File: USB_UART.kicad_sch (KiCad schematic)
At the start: 2 parts, among them U4 FT232RL

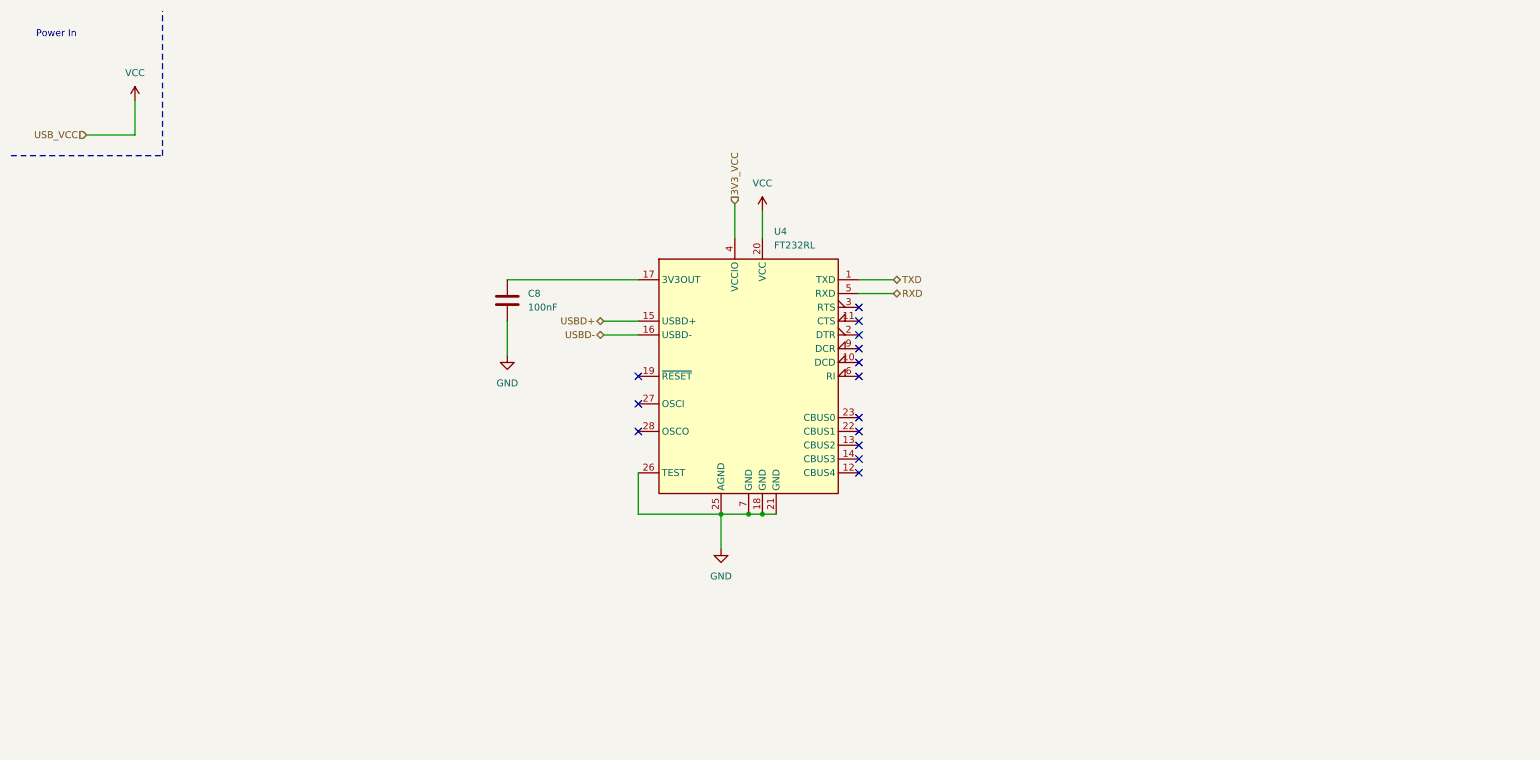
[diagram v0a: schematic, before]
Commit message: feat(usb-uart): add FT232RL for USB-serial, update schematic and layout
Added FT232RL USB‑to‑UART interface IC, powered from 3.3 V and 5 V rails. Connected RXD and TXD to MCU via hierarchical sheet. Left RS‑232 control lines and CBUS pins unconnected. Updated hierarchy with USB_UART sheet pins.

BREAKING CHANGE: USB connector moved to USB_UART sheet; schematic wiring changed to bus-based layout. AGND now kept in separate plane using GNDA power symbol in KiCad.
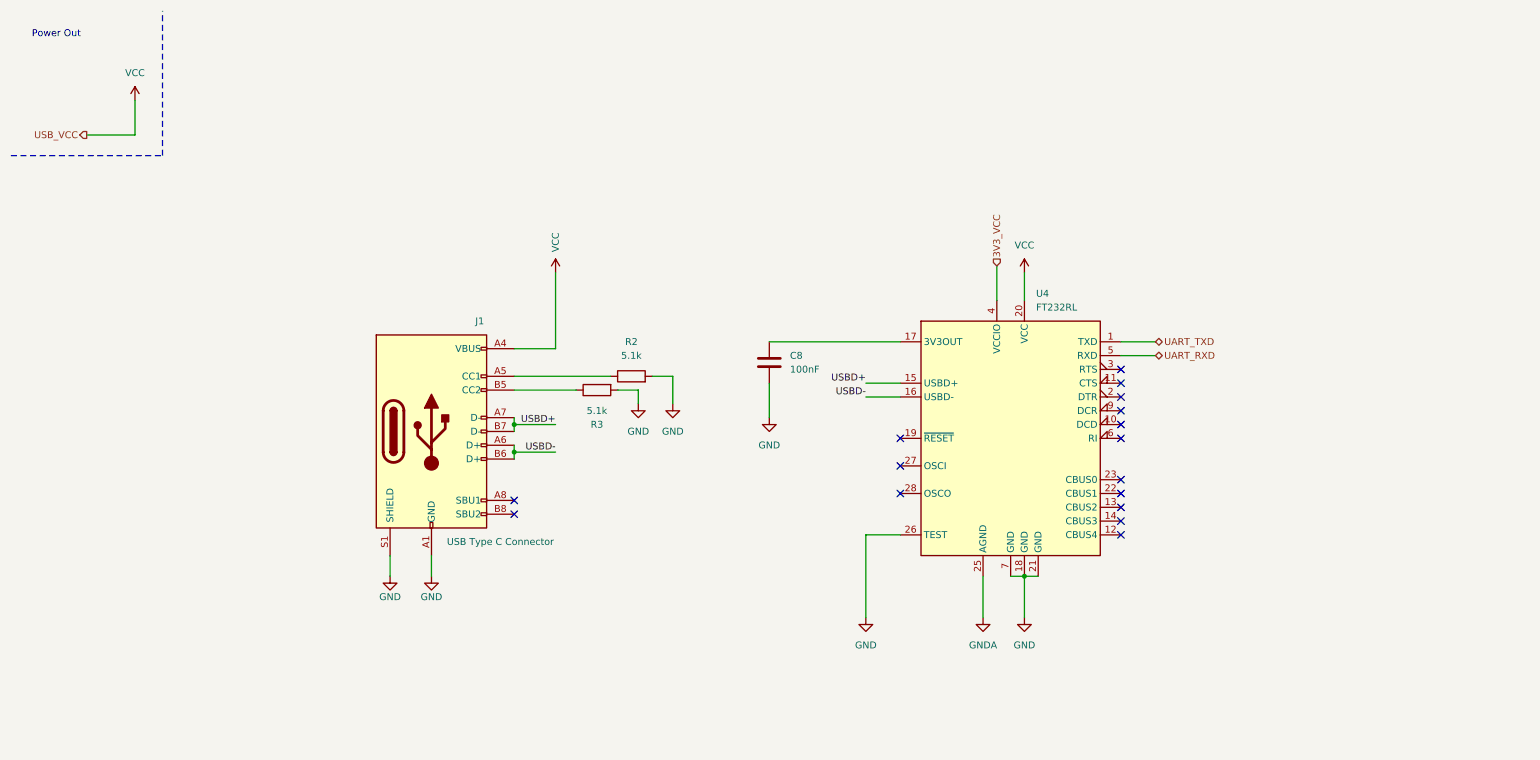
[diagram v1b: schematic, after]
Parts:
- added J1: USB Type C Connector, symbol Connector:USB_C_Receptacle_USB2.0_16P
- added R2, R3: 5.1k, symbol Device:R
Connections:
- net GND: now also J1.A1 (GND), J1.A12 (GND), J1.B1 (GND), J1.B12 (GND), J1.S1 (SHIELD), R2.2, R3.2; no longer U4.25 (AGND)
- net USBD+: now also J1.A7 (D-), J1.B7 (D-)
- net USBD-: now also J1.A6 (D+), J1.B6 (D+)
- net VCC: now also J1.A4 (VBUS), J1.A9 (VBUS), J1.B4 (VBUS), J1.B9 (VBUS)
- net RXD renamed UART_RXD
- net TXD renamed UART_TXD
- new net: J1.A5 (CC1), R2.1
- new net: J1.B5 (CC2), R3.1
- new net GNDA: U4.25 (AGND)
- no-connect marks 14 -> 16
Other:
- note added: "Power Out"
- note removed: "Power In"
- moved on the sheet: C8, U4

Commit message: fix: Separted CC1 and CC2 resistors and fixed the UART label directions
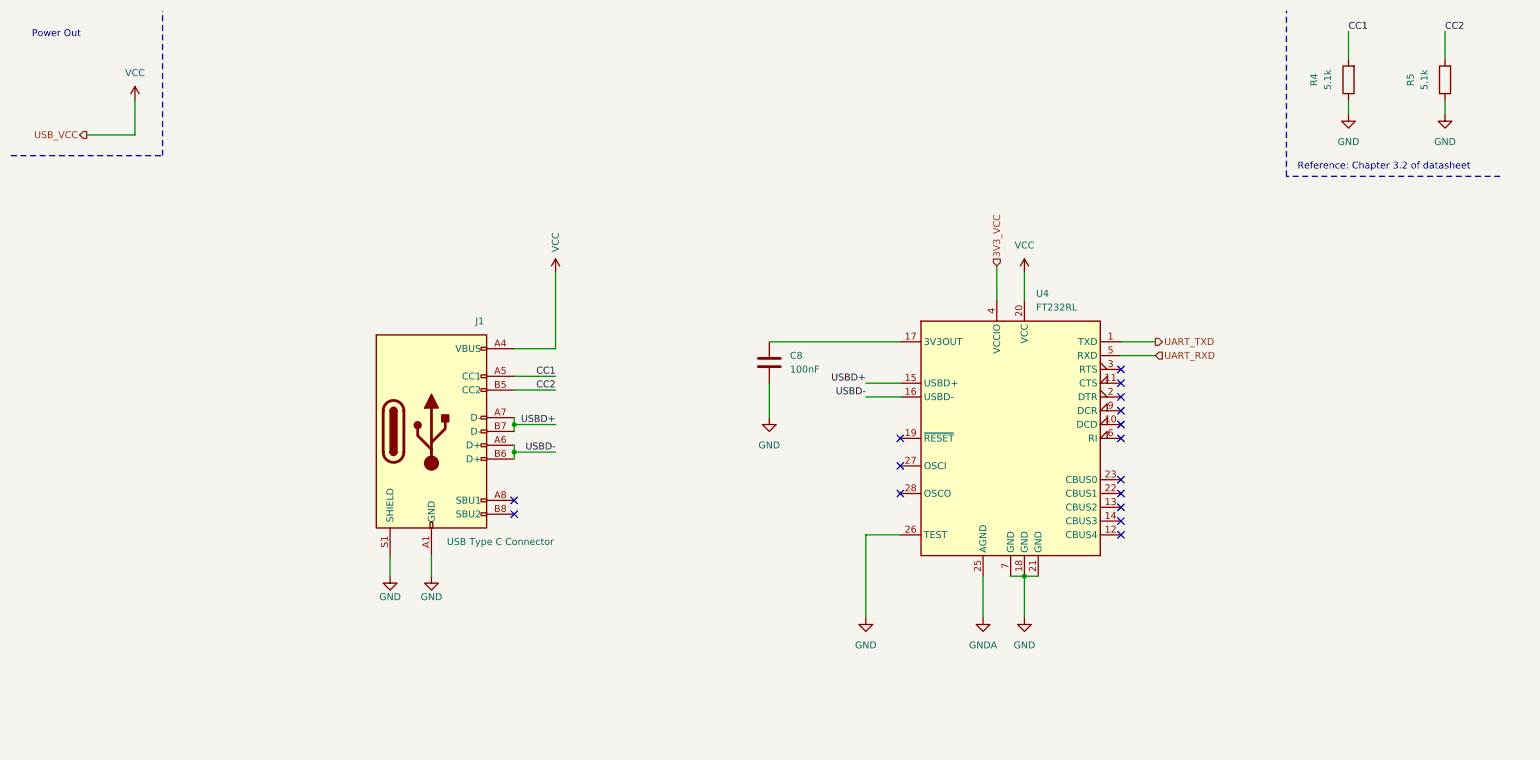
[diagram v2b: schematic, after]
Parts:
- removed R2, R3: 5.1k, symbol Device:R
- added R4, R5: 5.1k, symbol Device:R
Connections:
- net GND: now also R4.1, R5.1
- net CC1: now reaches J1.A5 (CC1)
- net CC1: now also R4.2
- net CC2: now reaches J1.B5 (CC2)
- net CC2: now also R5.2
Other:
- note added: "Reference: Chapter 3.2 of datasheet"

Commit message: feat: added footprints for the 5.1k resistors
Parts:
- C8: footprint (none) -> Capacitor_SMD:C_0603_1608Metric_Pad1.08x0.95mm_HandSolder
- R4, R5: footprint (none) -> Resistor_SMD:R_0603_1608Metric_Pad0.98x0.95mm_HandSolder
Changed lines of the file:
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@@
 			)
 		)
-		(property "Footprint" ""
+		(property "Footprint" "Resistor_SMD:R_0603_1608Metric_Pad0.98x0.95mm_HandSolder"
 			(at 276.098 25.4 90)
 			(effects
@@
 			)
 		)
-		(property "Footprint" ""
+		(property "Footprint" "Resistor_SMD:R_0603_1608Metric_Pad0.98x0.95mm_HandSolder"
 			(at 258.318 25.4 90)
 			(effects
@@
 			)
 		)
-		(property "Footprint" ""
+		(property "Footprint" "Capacitor_SMD:C_0603_1608Metric_Pad1.08x0.95mm_HandSolder"
 			(at 150.8252 81.28 0)
 			(effects

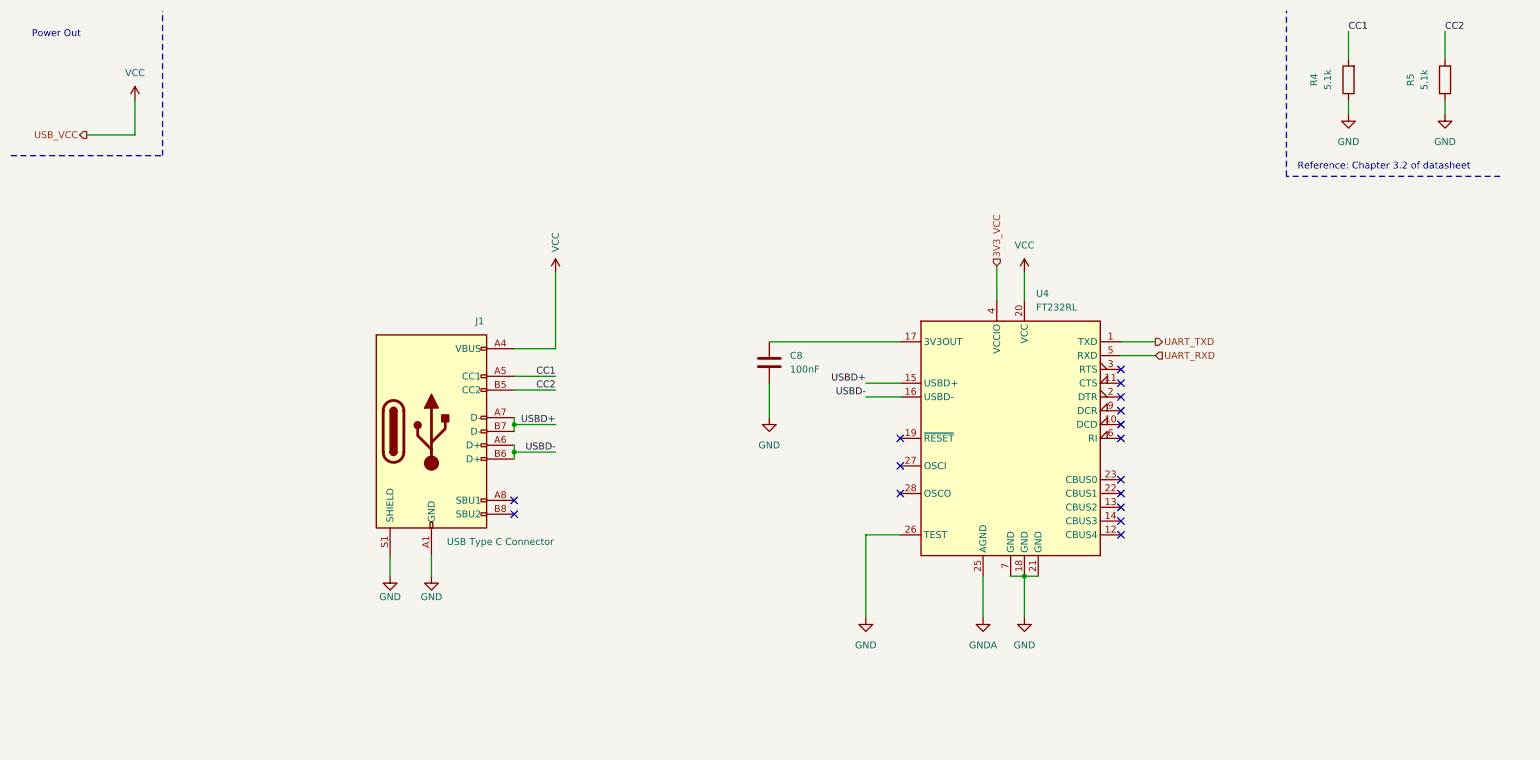
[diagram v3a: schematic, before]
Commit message: feat(FT232RL_Reset): Added FT232RL Reset functionality using the Reset switch
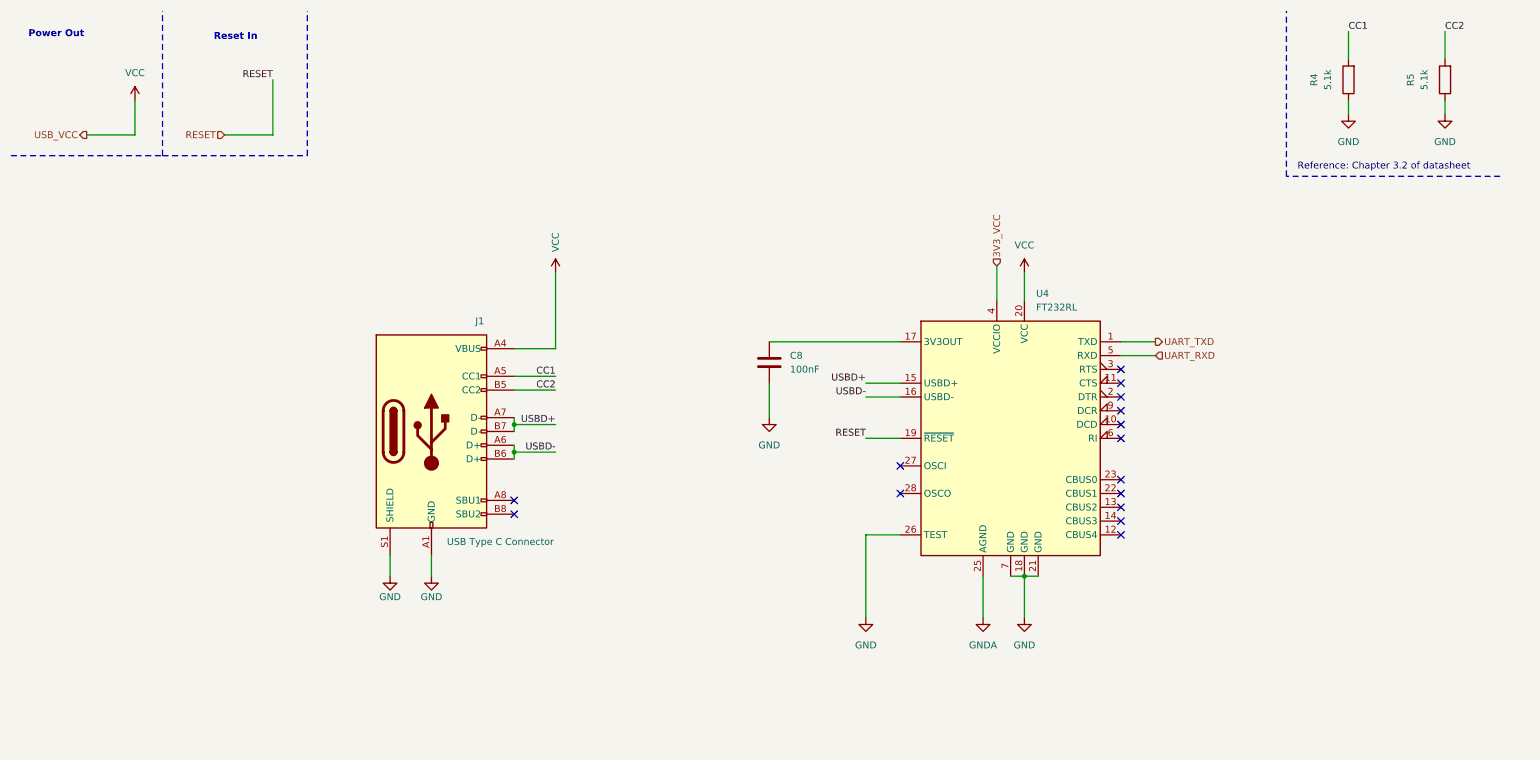
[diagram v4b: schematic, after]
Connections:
- net RESET: now reaches U4.19 (~{RESET})
- no-connect marks 16 -> 15
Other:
- note added: "Reset In"
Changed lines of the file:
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@@
+		)
+	)
+	(text "Reset In\n"
+		(exclude_from_sim no)
+		(at 51.562 17.526 0)
+		(effects
+			(font
+				(size 1.27 1.27)
+				(thickness 0.254)
+				(bold yes)
+				(color 0 0 0 1)
+			)
 		)
 	)
@@
 			(font
 				(size 1.27 1.27)
-				(thickness 0.1588)
+				(thickness 0.254)
+				(bold yes)
 				(color 0 0 0 1)
 			)
@@
 	)
 	(no_connect
-		(at 173.99 91.44)
-	)
-	(no_connect
 		(at 102.87 102.87)
 	)
@@
 		)
 	)
-	(wire
-		(pts
-			(xy 196.85 60.96) (xy 196.85 66.04)
-		)
-		(stroke
-			(width 0)
-			(type default)
-		)
-	)
-	(wire
-		(pts
-			(xy 110.49 74.93) (xy 102.87 74.93)
-		)
-		(stroke
-			(width 0)
-			(type default)
-		)
-	)
 	(polyline
 		(pts
-			(xy 284.48 43.18) (xy 245.11 43.18)
+			(xy 64.77 39.37) (xy 64.77 12.7)
 		)
 		(stroke
@@
 	(wire
 		(pts
-			(xy 24.13 35.56) (xy 33.02 35.56)
-		)
-		(stroke
-			(width 0)
-			(type default)
-		)
-	)
-	(wire
-		(pts
-			(xy 189.23 116.84) (xy 189.23 124.46)
-		)
-		(stroke
-			(width 0)
-			(type default)
-		)
-	)
-	(wire
-		(pts
-			(xy 256.54 29.21) (xy 256.54 31.75)
-		)
-		(stroke
-			(width 0)
-			(type default)
-		)
-	)
-	(wire
-		(pts
-			(xy 167.64 109.22) (xy 167.64 124.46)
-		)
-		(stroke
-			(width 0)
-			(type default)
-		)
-	)
-	(wire
-		(pts
-			(xy 33.02 29.21) (xy 33.02 35.56)
-		)
-		(stroke
-			(width 0)
-			(type default)
-		)
-	)
-	(wire
-		(pts
-			(xy 167.64 109.22) (xy 173.99 109.22)
-		)
-		(stroke
-			(width 0)
-			(type default)
-		)
-	)
-	(wire
-		(pts
-			(xy 149.86 73.66) (xy 173.99 73.66)
-		)
-		(stroke
-			(width 0)
-			(type default)
-		)
-	)
-	(wire
-		(pts
-			(xy 256.54 16.51) (xy 256.54 21.59)
-		)
-		(stroke
-			(width 0)
-			(type default)
-		)
-	)
-	(wire
-		(pts
-			(xy 80.01 113.03) (xy 80.01 116.84)
+			(xy 196.85 60.96) (xy 196.85 66.04)
+		)
+		(stroke
+			(width 0)
+			(type default)
+		)
+	)
+	(wire
+		(pts
+			(xy 110.49 74.93) (xy 102.87 74.93)
 		)
 		(stroke
@@
 	(polyline
 		(pts
-			(xy 10.16 39.37) (xy 38.1 39.37)
+			(xy 284.48 43.18) (xy 245.11 43.18)
 		)
 		(stroke
@@
 	(wire
 		(pts
-			(xy 102.87 87.63) (xy 102.87 88.9)
-		)
-		(stroke
-			(width 0)
-			(type default)
-		)
-	)
-	(wire
-		(pts
-			(xy 194.31 116.84) (xy 196.85 116.84)
-		)
-		(stroke
-			(width 0)
-			(type default)
-		)
-	)
-	(wire
-		(pts
-			(xy 102.87 80.01) (xy 110.49 80.01)
-		)
-		(stroke
-			(width 0)
-			(type default)
-		)
-	)
-	(wire
-		(pts
-			(xy 274.32 16.51) (xy 274.32 21.59)
-		)
-		(stroke
-			(width 0)
-			(type default)
-		)
-	)
-	(wire
-		(pts
-			(xy 102.87 88.9) (xy 102.87 90.17)
-		)
-		(stroke
-			(width 0)
-			(type default)
-		)
-	)
-	(wire
-		(pts
-			(xy 102.87 92.71) (xy 102.87 93.98)
+			(xy 24.13 35.56) (xy 33.02 35.56)
+		)
+		(stroke
+			(width 0)
+			(type default)
+		)
+	)
+	(wire
+		(pts
+			(xy 58.42 35.56) (xy 49.53 35.56)
+		)
+		(stroke
+			(width 0)
+			(type default)
+		)
+	)
+	(wire
+		(pts
+			(xy 189.23 116.84) (xy 189.23 124.46)
+		)
+		(stroke
+			(width 0)
+			(type default)
+		)
+	)
+	(wire
+		(pts
+			(xy 256.54 29.21) (xy 256.54 31.75)
+		)
+		(stroke
+			(width 0)
+			(type default)
+		)
+	)
+	(wire
+		(pts
+			(xy 167.64 109.22) (xy 167.64 124.46)
+		)
+		(stroke
+			(width 0)
+			(type default)
+		)
+	)
+	(wire
+		(pts
+			(xy 33.02 29.21) (xy 33.02 35.56)
+		)
+		(stroke
+			(width 0)
+			(type default)
+		)
+	)
+	(wire
+		(pts
+			(xy 58.42 25.4) (xy 58.42 35.56)
+		)
+		(stroke
+			(width 0)
+			(type default)
+		)
+	)
+	(wire
+		(pts
+			(xy 167.64 109.22) (xy 173.99 109.22)
+		)
+		(stroke
+			(width 0)
+			(type default)
+		)
+	)
+	(wire
+		(pts
+			(xy 149.86 73.66) (xy 173.99 73.66)
+		)
+		(stroke
+			(width 0)
+			(type default)
+		)
+	)
+	(wire
+		(pts
+			(xy 256.54 16.51) (xy 256.54 21.59)
+		)
+		(stroke
+			(width 0)
+			(type default)
+		)
+	)
+	(wire
+		(pts
+			(xy 80.01 113.03) (xy 80.01 116.84)
 		)
 		(stroke
@@
 	(polyline
 		(pts
-			(xy 245.11 43.18) (xy 245.11 12.7)
+			(xy 10.16 39.37) (xy 38.1 39.37)
 		)
 		(stroke
@@
 	(wire
 		(pts
+			(xy 102.87 87.63) (xy 102.87 88.9)
+		)
+		(stroke
+			(width 0)
+			(type default)
+		)
+	)
+	(wire
+		(pts
+			(xy 194.31 116.84) (xy 196.85 116.84)
+		)
+		(stroke
+			(width 0)
+			(type default)
+		)
+	)
+	(wire
+		(pts
+			(xy 102.87 80.01) (xy 110.49 80.01)
+		)
+		(stroke
+			(width 0)
+			(type default)
+		)
+	)
+	(wire
+		(pts
+			(xy 274.32 16.51) (xy 274.32 21.59)
+		)
+		(stroke
+			(width 0)
+			(type default)
+		)
+	)
+	(polyline
+		(pts
+			(xy 38.1 39.37) (xy 64.77 39.37)
+		)
+		(stroke
+			(width 0)
+			(type dash)
+			(color 72 72 72 1)
+		)
+	)
+	(wire
+		(pts
+			(xy 102.87 88.9) (xy 102.87 90.17)
+		)
+		(stroke
+			(width 0)
+			(type default)
+		)
+	)
+	(wire
+		(pts
+			(xy 102.87 92.71) (xy 102.87 93.98)
+		)
+		(stroke
+			(width 0)
+			(type default)
+		)
+	)
+	(polyline
+		(pts
+			(xy 245.11 43.18) (xy 245.11 12.7)
+		)
+		(stroke
+			(width 0)
+			(type dash)
+			(color 72 72 72 1)
+		)
+	)
+	(wire
+		(pts
 			(xy 87.63 113.03) (xy 87.63 116.84)
+		)
+		(stroke
+			(width 0)
+			(type default)
+		)
+	)
+	(wire
+		(pts
+			(xy 167.64 91.44) (xy 173.99 91.44)
 		)
 		(stroke
@@
 		)
 	)
+	(label "RESET"
+		(at 58.42 25.4 180)
+		(effects
+			(font
+				(size 1.27 1.27)
+			)
+			(justify right bottom)
+		)
+	)
 	(label "CC1"
 		(at 256.54 16.51 0)
@@
 	(label "USBD+"
 		(at 167.64 81.28 180)
+		(effects
+			(font
+				(size 1.27 1.27)
+			)
+			(justify right bottom)
+		)
+	)
+	(label "RESET"
+		(at 167.64 91.44 180)
 		(effects
 			(font
@@
 		)
 	)
+	(hierarchical_label "RESET"
+		(shape input)
+		(at 49.53 35.56 180)
+		(effects
+			(font
+				(size 1.27 1.27)
+			)
+			(justify right)
+		)
+	)
